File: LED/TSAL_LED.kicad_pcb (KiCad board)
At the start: 2 copper layers, 104.1 x 45.8 mm, 70 parts, among them J1 Mini-SPOX, Q1 Q_PMOS_GSD, U2 XC9141

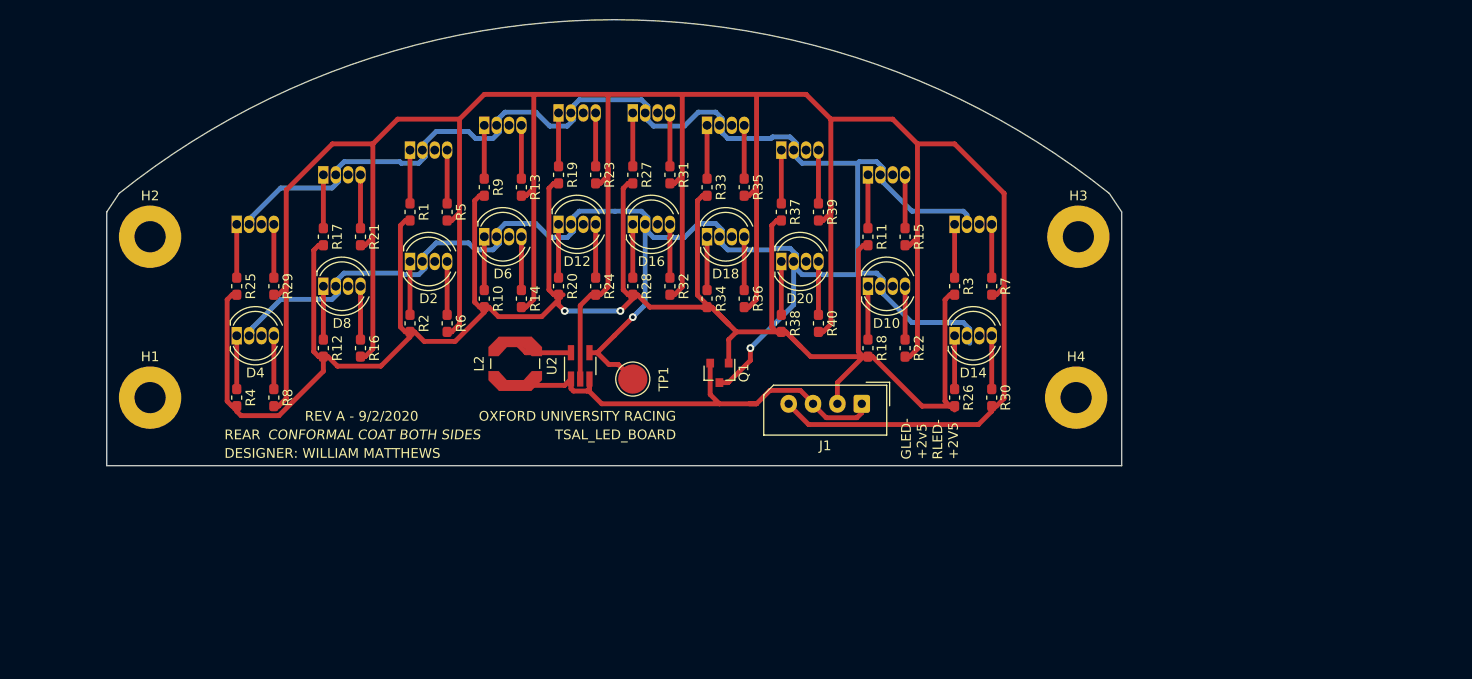
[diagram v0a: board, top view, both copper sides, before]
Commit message: Move LED board files
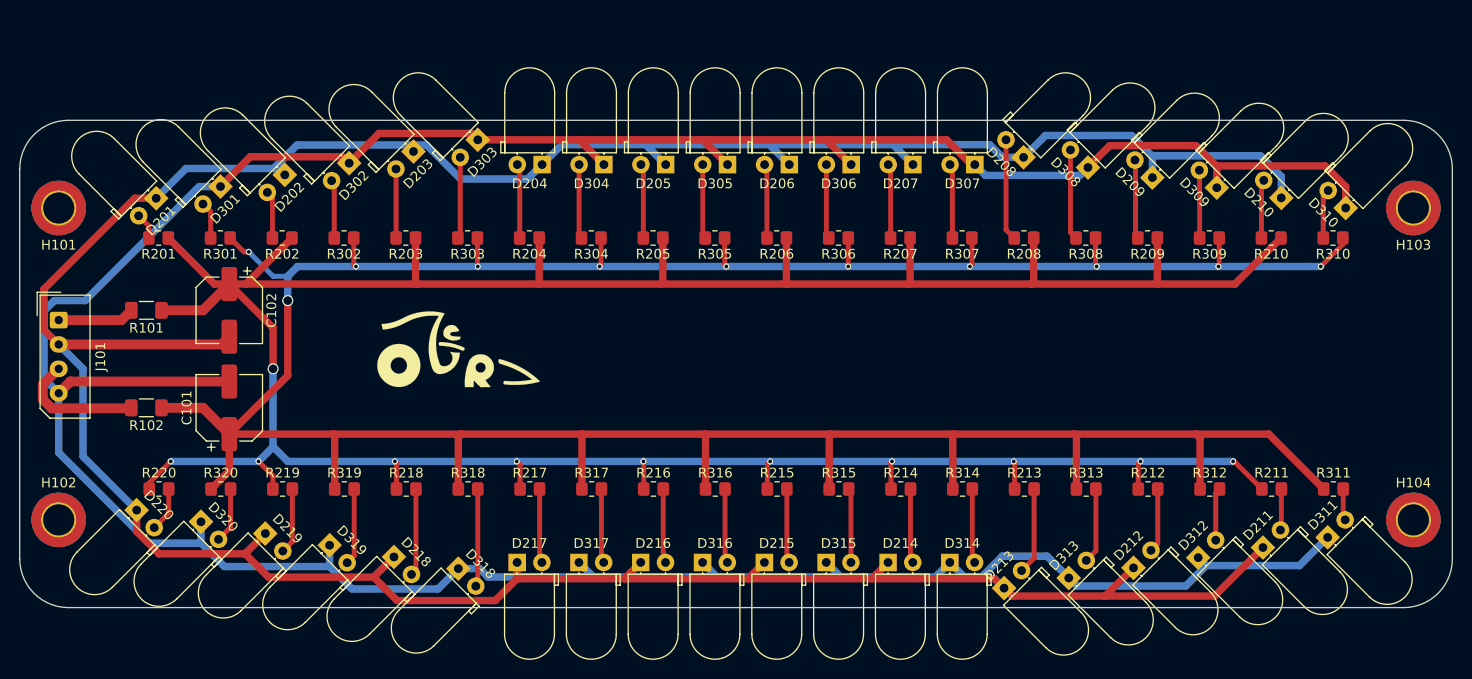
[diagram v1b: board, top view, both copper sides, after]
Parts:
- removed D1, D10, D11, D12, D13, D14, D15, D16, D17, D18, D19, D2, D20, D3, D4, D5, D6, D7, D8, D9: LED_RABG, LED_THT:LED_D5.0mm-4_RGB
- removed the G*** at (125.1, 76.8)
- removed H1, H2, H3, H4: MountingHole, MountingHole:MountingHole_3.2mm_M3_Pad
- removed J1: Mini-SPOX, Connector_Molex:Molex_SPOX_5267-04A_1x04_P2.50mm_Vertical
- removed L2: 4.7uH, Inductor_SMD:L_Coilcraft_LPS5030
- removed Q1: Q_PMOS_GSD, Package_TO_SOT_SMD:SOT-23
- removed R1, R10, R11, R12, R17, R18, R19, R2, R20, R25, R26, R27, R28, R3, R33, R34, R37, R38, R4, R9: 15R, Resistor_SMD:R_0603_1608Metric_Pad1.05x0.95mm_HandSolder
- removed R13, R14, R15, R16, R21, R22, R29, R30, R35, R36, R7, R8: 39R, Resistor_SMD:R_0603_1608Metric_Pad1.05x0.95mm_HandSolder
- removed R23, R24, R31, R32, R39, R40, R5, R6: DNP, Resistor_SMD:R_0603_1608Metric_Pad1.05x0.95mm_HandSolder
- removed TP1: TestPoint, TestPoint:TestPoint_Pad_D3.0mm
- removed U2: XC9141, Package_TO_SOT_SMD:SOT-23-5_HandSoldering
- added C101: 100u, Capacitor_SMD:CP_Elec_6.3x5.8, F.Cu at (87.5, 85.5)
- added C102: 100u, Capacitor_SMD:CP_Elec_6.3x5.8, F.Cu at (87.5, 75.5)
- added D201: LED, LED_THT:LED_D5.0mm_Horizontal_O1.27mm_Z3.0mm, F.Cu at (80.0, 64.0)
- added D202: LED, LED_THT:LED_D5.0mm_Horizontal_O1.27mm_Z3.0mm, F.Cu at (93.2, 61.6)
- added D203: LED, LED_THT:LED_D5.0mm_Horizontal_O1.27mm_Z3.0mm, F.Cu at (106.4, 59.2)
- added D204: LED, LED_THT:LED_D5.0mm_Horizontal_O1.27mm_Z3.0mm, F.Cu at (119.6, 60.5)
- added D205: LED, LED_THT:LED_D5.0mm_Horizontal_O1.27mm_Z3.0mm, F.Cu at (132.3, 60.5)
- added D206: LED, LED_THT:LED_D5.0mm_Horizontal_O1.27mm_Z3.0mm, F.Cu at (145.0, 60.5)
- added D207: LED, LED_THT:LED_D5.0mm_Horizontal_O1.27mm_Z3.0mm, F.Cu at (157.7, 60.5)
- added D208: LED, LED_THT:LED_D5.0mm_Horizontal_O1.27mm_Z3.0mm, F.Cu at (169.0, 59.8)
- added D209: LED, LED_THT:LED_D5.0mm_Horizontal_O1.27mm_Z3.0mm, F.Cu at (182.2, 61.9)
- added D210: LED, LED_THT:LED_D5.0mm_Horizontal_O1.27mm_Z3.0mm, F.Cu at (195.4, 64.0)
- added D211: LED, LED_THT:LED_D5.0mm_Horizontal_O1.27mm_Z3.0mm, F.Cu at (193.6, 99.8)
- added D212: LED, LED_THT:LED_D5.0mm_Horizontal_O1.27mm_Z3.0mm, F.Cu at (180.3, 101.9)
- added D213: LED, LED_THT:LED_D5.0mm_Horizontal_O1.27mm_Z3.0mm, F.Cu at (167.0, 104.0)
- added D214: LED, LED_THT:LED_D5.0mm_Horizontal_O1.27mm_Z3.0mm, F.Cu at (155.1, 101.4)
- added D215: LED, LED_THT:LED_D5.0mm_Horizontal_O1.27mm_Z3.0mm, F.Cu at (142.4, 101.4)
- added D216: LED, LED_THT:LED_D5.0mm_Horizontal_O1.27mm_Z3.0mm, F.Cu at (129.7, 101.4)
- added D217: LED, LED_THT:LED_D5.0mm_Horizontal_O1.27mm_Z3.0mm, F.Cu at (117.0, 101.4)
- added D218: LED, LED_THT:LED_D5.0mm_Horizontal_O1.27mm_Z3.0mm, F.Cu at (104.4, 100.8)
- added D219: LED, LED_THT:LED_D5.0mm_Horizontal_O1.27mm_Z3.0mm, F.Cu at (91.2, 98.4)
- added D220: LED, LED_THT:LED_D5.0mm_Horizontal_O1.27mm_Z3.0mm, F.Cu at (78.0, 96.0)
- added D301: LED, LED_THT:LED_D5.0mm_Horizontal_O1.27mm_Z3.0mm, F.Cu at (86.6, 62.8)
- added D302: LED, LED_THT:LED_D5.0mm_Horizontal_O1.27mm_Z3.0mm, F.Cu at (99.8, 60.4)
- added D303: LED, LED_THT:LED_D5.0mm_Horizontal_O1.27mm_Z3.0mm, F.Cu at (113.0, 58.0)
- added D304: LED, LED_THT:LED_D5.0mm_Horizontal_O1.27mm_Z3.0mm, F.Cu at (125.9, 60.5)
- added D305: LED, LED_THT:LED_D5.0mm_Horizontal_O1.27mm_Z3.0mm, F.Cu at (138.6, 60.5)
- added D306: LED, LED_THT:LED_D5.0mm_Horizontal_O1.27mm_Z3.0mm, F.Cu at (151.3, 60.5)
- added D307: LED, LED_THT:LED_D5.0mm_Horizontal_O1.27mm_Z3.0mm, F.Cu at (164.0, 60.5)
- added D308: LED, LED_THT:LED_D5.0mm_Horizontal_O1.27mm_Z3.0mm, F.Cu at (175.6, 60.8)
- added D309: LED, LED_THT:LED_D5.0mm_Horizontal_O1.27mm_Z3.0mm, F.Cu at (188.8, 62.9)
- added D310: LED, LED_THT:LED_D5.0mm_Horizontal_O1.27mm_Z3.0mm, F.Cu at (202.1, 65.0)
- added D311: LED, LED_THT:LED_D5.0mm_Horizontal_O1.27mm_Z3.0mm, F.Cu at (200.2, 98.8)
- added D312: LED, LED_THT:LED_D5.0mm_Horizontal_O1.27mm_Z3.0mm, F.Cu at (186.9, 100.9)
- added D313: LED, LED_THT:LED_D5.0mm_Horizontal_O1.27mm_Z3.0mm, F.Cu at (173.6, 103.0)
- added D314: LED, LED_THT:LED_D5.0mm_Horizontal_O1.27mm_Z3.0mm, F.Cu at (161.4, 101.4)
- added D315: LED, LED_THT:LED_D5.0mm_Horizontal_O1.27mm_Z3.0mm, F.Cu at (148.8, 101.4)
- added D316: LED, LED_THT:LED_D5.0mm_Horizontal_O1.27mm_Z3.0mm, F.Cu at (136.1, 101.4)
- added D317: LED, LED_THT:LED_D5.0mm_Horizontal_O1.27mm_Z3.0mm, F.Cu at (123.4, 101.4)
- added D318: LED, LED_THT:LED_D5.0mm_Horizontal_O1.27mm_Z3.0mm, F.Cu at (111.0, 102.0)
- added D319: LED, LED_THT:LED_D5.0mm_Horizontal_O1.27mm_Z3.0mm, F.Cu at (97.8, 99.6)
- added D320: LED, LED_THT:LED_D5.0mm_Horizontal_O1.27mm_Z3.0mm, F.Cu at (84.6, 97.2)
- added G***: LOGO, TSAL_LED_V2:OUR_logo_20x10mm, F.Cu at (111.0, 79.5)
- added H101: MountingHole, MountingHole:MountingHole_3.2mm_M3_DIN965_Pad_TopBottom, F.Cu at (70.0, 65.0)
- added H102: MountingHole, MountingHole:MountingHole_3.2mm_M3_DIN965_Pad_TopBottom, F.Cu at (70.0, 97.0)
- added H103: MountingHole, MountingHole:MountingHole_3.2mm_M3_DIN965_Pad_TopBottom, F.Cu at (209.0, 65.0)
- added H104: MountingHole, MountingHole:MountingHole_3.2mm_M3_DIN965_Pad_TopBottom, F.Cu at (209.0, 97.0)
- added J101: Conn_01x04_Male, Connector_Molex:Molex_SPOX_5267-04A_1x04_P2.50mm_Vertical, F.Cu at (70.0, 76.5)
- added R101: TUNE, <100R, Resistor_SMD:R_1206_3216Metric_Pad1.30x1.75mm_HandSolder, F.Cu at (79.0, 75.5)
- added R102: TUNE, <300R, Resistor_SMD:R_1206_3216Metric_Pad1.30x1.75mm_HandSolder, F.Cu at (79.0, 85.5)
- added R201: 33R, Resistor_SMD:R_0805_2012Metric_Pad1.20x1.40mm_HandSolder, F.Cu at (80.2, 68.1)
- added R202: 33R, Resistor_SMD:R_0805_2012Metric_Pad1.20x1.40mm_HandSolder, F.Cu at (92.9, 68.1)
- added R203: 33R, Resistor_SMD:R_0805_2012Metric_Pad1.20x1.40mm_HandSolder, F.Cu at (105.6, 68.1)
- added R204: 33R, Resistor_SMD:R_0805_2012Metric_Pad1.20x1.40mm_HandSolder, F.Cu at (118.3, 68.1)
- added R205: 33R, Resistor_SMD:R_0805_2012Metric_Pad1.20x1.40mm_HandSolder, F.Cu at (131.0, 68.1)
- added R206: 33R, Resistor_SMD:R_0805_2012Metric_Pad1.20x1.40mm_HandSolder, F.Cu at (143.7, 68.1)
- added R207: 33R, Resistor_SMD:R_0805_2012Metric_Pad1.20x1.40mm_HandSolder, F.Cu at (156.4, 68.1)
- added R208: 33R, Resistor_SMD:R_0805_2012Metric_Pad1.20x1.40mm_HandSolder, F.Cu at (169.0, 68.1)
- added R209: 33R, Resistor_SMD:R_0805_2012Metric_Pad1.20x1.40mm_HandSolder, F.Cu at (181.7, 68.1)
- added R210: 33R, Resistor_SMD:R_0805_2012Metric_Pad1.20x1.40mm_HandSolder, F.Cu at (194.4, 68.1)
- added R211: 33R, Resistor_SMD:R_0805_2012Metric_Pad1.20x1.40mm_HandSolder, F.Cu at (194.5, 93.8)
- added R212: 33R, Resistor_SMD:R_0805_2012Metric_Pad1.20x1.40mm_HandSolder, F.Cu at (181.8, 93.8)
- added R213: 33R, Resistor_SMD:R_0805_2012Metric_Pad1.20x1.40mm_HandSolder, F.Cu at (169.1, 93.8)
- added R214: 33R, Resistor_SMD:R_0805_2012Metric_Pad1.20x1.40mm_HandSolder, F.Cu at (156.4, 93.8)
- added R215: 33R, Resistor_SMD:R_0805_2012Metric_Pad1.20x1.40mm_HandSolder, F.Cu at (143.7, 93.8)
- added R216: 33R, Resistor_SMD:R_0805_2012Metric_Pad1.20x1.40mm_HandSolder, F.Cu at (131.0, 93.8)
- added R217: 33R, Resistor_SMD:R_0805_2012Metric_Pad1.20x1.40mm_HandSolder, F.Cu at (118.3, 93.8)
- added R218: 33R, Resistor_SMD:R_0805_2012Metric_Pad1.20x1.40mm_HandSolder, F.Cu at (105.7, 93.8)
- added R219: 33R, Resistor_SMD:R_0805_2012Metric_Pad1.20x1.40mm_HandSolder, F.Cu at (93.0, 93.8)
- added R220: 33R, Resistor_SMD:R_0805_2012Metric_Pad1.20x1.40mm_HandSolder, F.Cu at (80.3, 93.8)
- added R301: 100R, Resistor_SMD:R_0805_2012Metric_Pad1.20x1.40mm_HandSolder, F.Cu at (86.6, 68.1)
- added R302: 100R, Resistor_SMD:R_0805_2012Metric_Pad1.20x1.40mm_HandSolder, F.Cu at (99.3, 68.1)
- added R303: 100R, Resistor_SMD:R_0805_2012Metric_Pad1.20x1.40mm_HandSolder, F.Cu at (112.0, 68.1)
- added R304: 100R, Resistor_SMD:R_0805_2012Metric_Pad1.20x1.40mm_HandSolder, F.Cu at (124.6, 68.1)
- added R305: 100R, Resistor_SMD:R_0805_2012Metric_Pad1.20x1.40mm_HandSolder, F.Cu at (137.3, 68.1)
- added R306: 100R, Resistor_SMD:R_0805_2012Metric_Pad1.20x1.40mm_HandSolder, F.Cu at (150.0, 68.1)
- added R307: 100R, Resistor_SMD:R_0805_2012Metric_Pad1.20x1.40mm_HandSolder, F.Cu at (162.7, 68.1)
- added R308: 100R, Resistor_SMD:R_0805_2012Metric_Pad1.20x1.40mm_HandSolder, F.Cu at (175.4, 68.1)
- added R309: 100R, Resistor_SMD:R_0805_2012Metric_Pad1.20x1.40mm_HandSolder, F.Cu at (188.1, 68.1)
- added R310: 100R, Resistor_SMD:R_0805_2012Metric_Pad1.20x1.40mm_HandSolder, F.Cu at (200.8, 68.1)
- added R311: 100R, Resistor_SMD:R_0805_2012Metric_Pad1.20x1.40mm_HandSolder, F.Cu at (200.8, 93.8)
- added R312: 100R, Resistor_SMD:R_0805_2012Metric_Pad1.20x1.40mm_HandSolder, F.Cu at (188.1, 93.8)
- added R313: 100R, Resistor_SMD:R_0805_2012Metric_Pad1.20x1.40mm_HandSolder, F.Cu at (175.4, 93.8)
- added R314: 100R, Resistor_SMD:R_0805_2012Metric_Pad1.20x1.40mm_HandSolder, F.Cu at (162.7, 93.8)
- added R315: 100R, Resistor_SMD:R_0805_2012Metric_Pad1.20x1.40mm_HandSolder, F.Cu at (150.1, 93.8)
- added R316: 100R, Resistor_SMD:R_0805_2012Metric_Pad1.20x1.40mm_HandSolder, F.Cu at (137.4, 93.8)
- added R317: 100R, Resistor_SMD:R_0805_2012Metric_Pad1.20x1.40mm_HandSolder, F.Cu at (124.7, 93.8)
- added R318: 100R, Resistor_SMD:R_0805_2012Metric_Pad1.20x1.40mm_HandSolder, F.Cu at (112.0, 93.8)
- added R319: 100R, Resistor_SMD:R_0805_2012Metric_Pad1.20x1.40mm_HandSolder, F.Cu at (99.3, 93.8)
- added R320: 100R, Resistor_SMD:R_0805_2012Metric_Pad1.20x1.40mm_HandSolder, F.Cu at (86.6, 93.8)
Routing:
- net /RED_LEDS/RLED+: track 0.00 -> 335.0 mm, vias 0 -> 11
- net /GRN_LEDS/GLED+: track 0.00 -> 326.7 mm, vias 0 -> 11
- net /LED+: track 240.5 -> 0.00 mm, vias 2 -> 0
- net /RLED-: track 232.3 -> 349.3 mm, vias 2 -> 0
- net +2V5: track 48.1 -> 0.00 mm
- net /GLED-: track 356.3 -> 342.2 mm
- net /RLED+: track 0.00 -> 13.3 mm
- net Net-(D208-Pad2): track 0.00 -> 10.4 mm
- net Net-(D318-Pad2): track 0.00 -> 10.0 mm
- net Net-(D308-Pad2): track 0.00 -> 9.27 mm
- net Net-(D218-Pad2): track 0.00 -> 8.95 mm
- net Net-(D213-Pad2): track 0.00 -> 8.91 mm
- net Net-(D303-Pad2): track 0.00 -> 8.38 mm
- net Net-(D209-Pad2): track 0.00 -> 8.12 mm
- net /GLED+: track 0.00 -> 7.86 mm
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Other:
- board size 104.1 x 45.8 mm -> 147 x 50 mm
- rule pad_to_mask_clearance: 0.051 -> 0
- board text removed: "CONFORMAL COAT BOTH SIDES"
- board text removed: "DESIGNER: WILLIAM MATTHEWS"
- board text removed: "GLED- +2v5 RLED- +2V5"
- board text removed: "OXFORD UNIVERSITY RACING"
- board text removed: "Oxford University Racing"
- board text removed: "REAR"
- board text removed: "REV A - 9/2/2020"
- board text removed: "TSAL_LED_BOARD"
